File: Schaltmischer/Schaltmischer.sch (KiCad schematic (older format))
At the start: 17 parts, among them P1 Power, P2 IN, P3 Takt, P4 OUT, P5 GND, P6 GND, P7 GND, P8 GND, T1 Übertrager, T2 Übertrager, U1 FST3125

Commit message: Sicherung vor Trafo wechsel im layout
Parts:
- removed C1: 10µ, Discret:C1V7H_2, symbol CP
- removed C2: 10n, Capacitors_SMD:C_1206_HandSoldering, symbol C
- added C1: 10n, Capacitors_SMD:C_1206_HandSoldering, symbol C
- added C2, C3: 1µ, Capacitors_SMD:C_1206_HandSoldering, symbol CP
- added C6: 10µ, Capacitors_SMD:C_1206_HandSoldering, symbol CP
- C5: renamed from C4; value 100n -> 10n
- T1, T2: symbol TRANSFORMER_1P_2S_2 -> TRANSFORMER_SP_1S_2
- renumbered C3 to C4, P5 to P4, P6 to P5, P7 to P6, P8 to P7, P4 to P8, R2 to R1, R1 to R2
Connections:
- net +5V: now also C6.1
- net GND: now also C1.2, C2.2, C3.2, C6.2
- net IN: now also T1.4 (S1); no longer T1.1 (AA)
- net OUT: now also T2.4 (S1); no longer T2.1 (AA)
- net at U1.11 (B), U1.8 (B): now also T2.1 (PR1); no longer T2.5 (SD)
- net at U1.12 (A), U1.2 (A): now also T1.1 (PR1); no longer T1.5 (SD)
- net at C4.1, R1.2, R2.1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: now also C1.1, C2.1, C3.1; no longer T1.4 (SB), T2.4 (SB)
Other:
- moved on the sheet: C4, R2

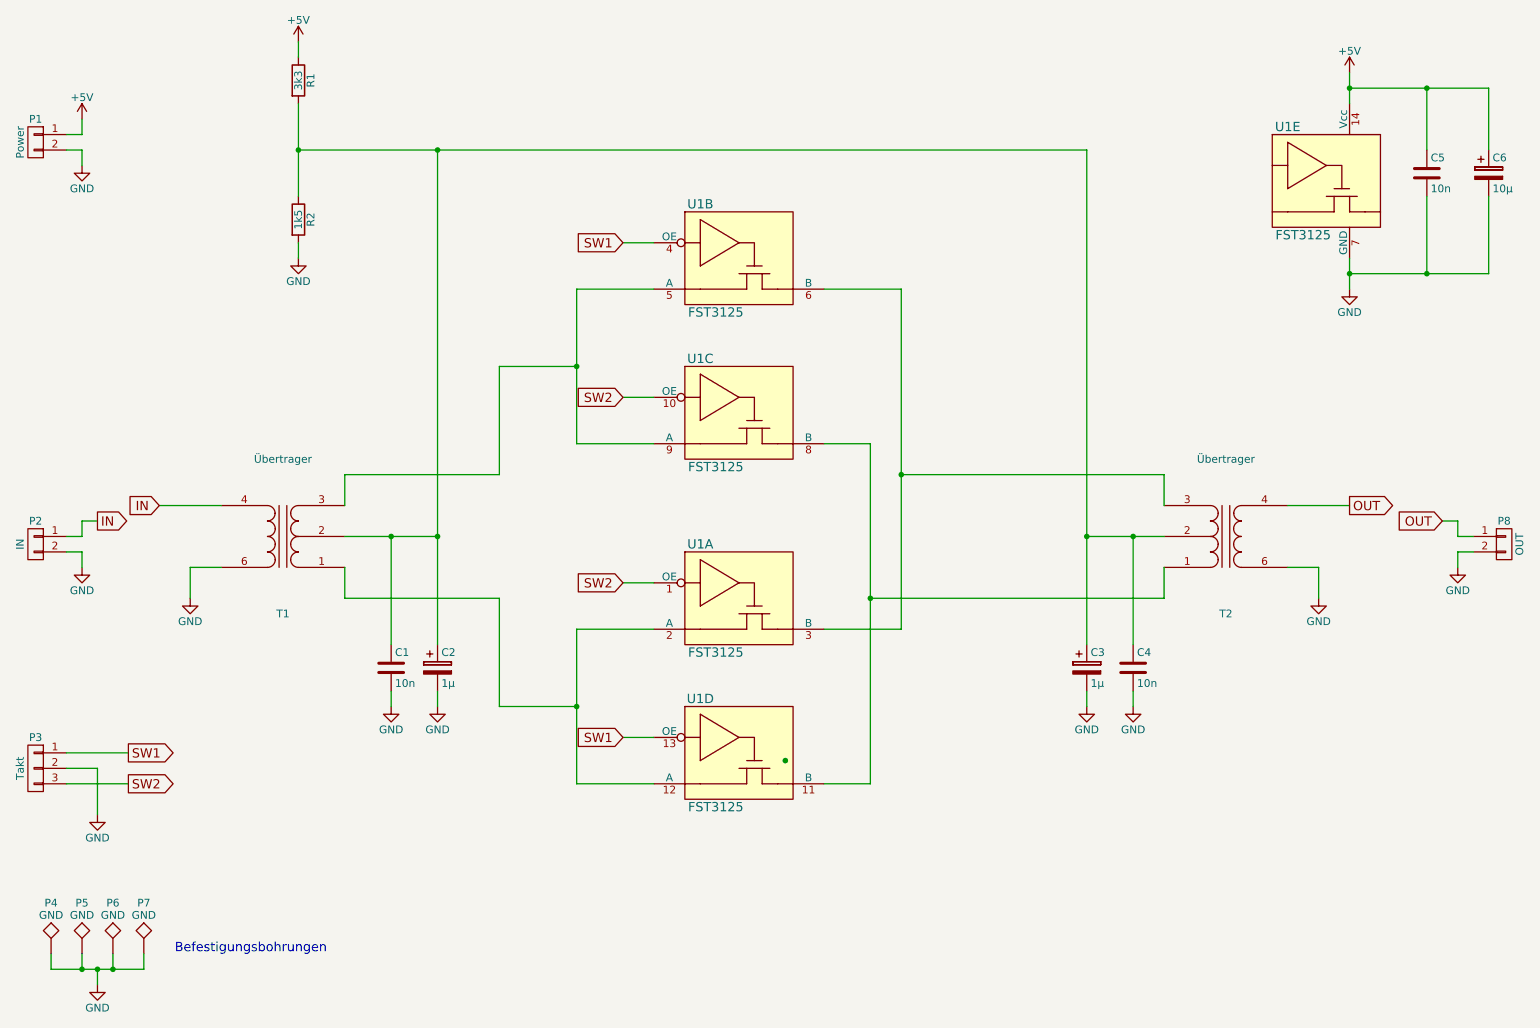
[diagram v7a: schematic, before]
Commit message: Schaltplan Rev E; Layout Rev B
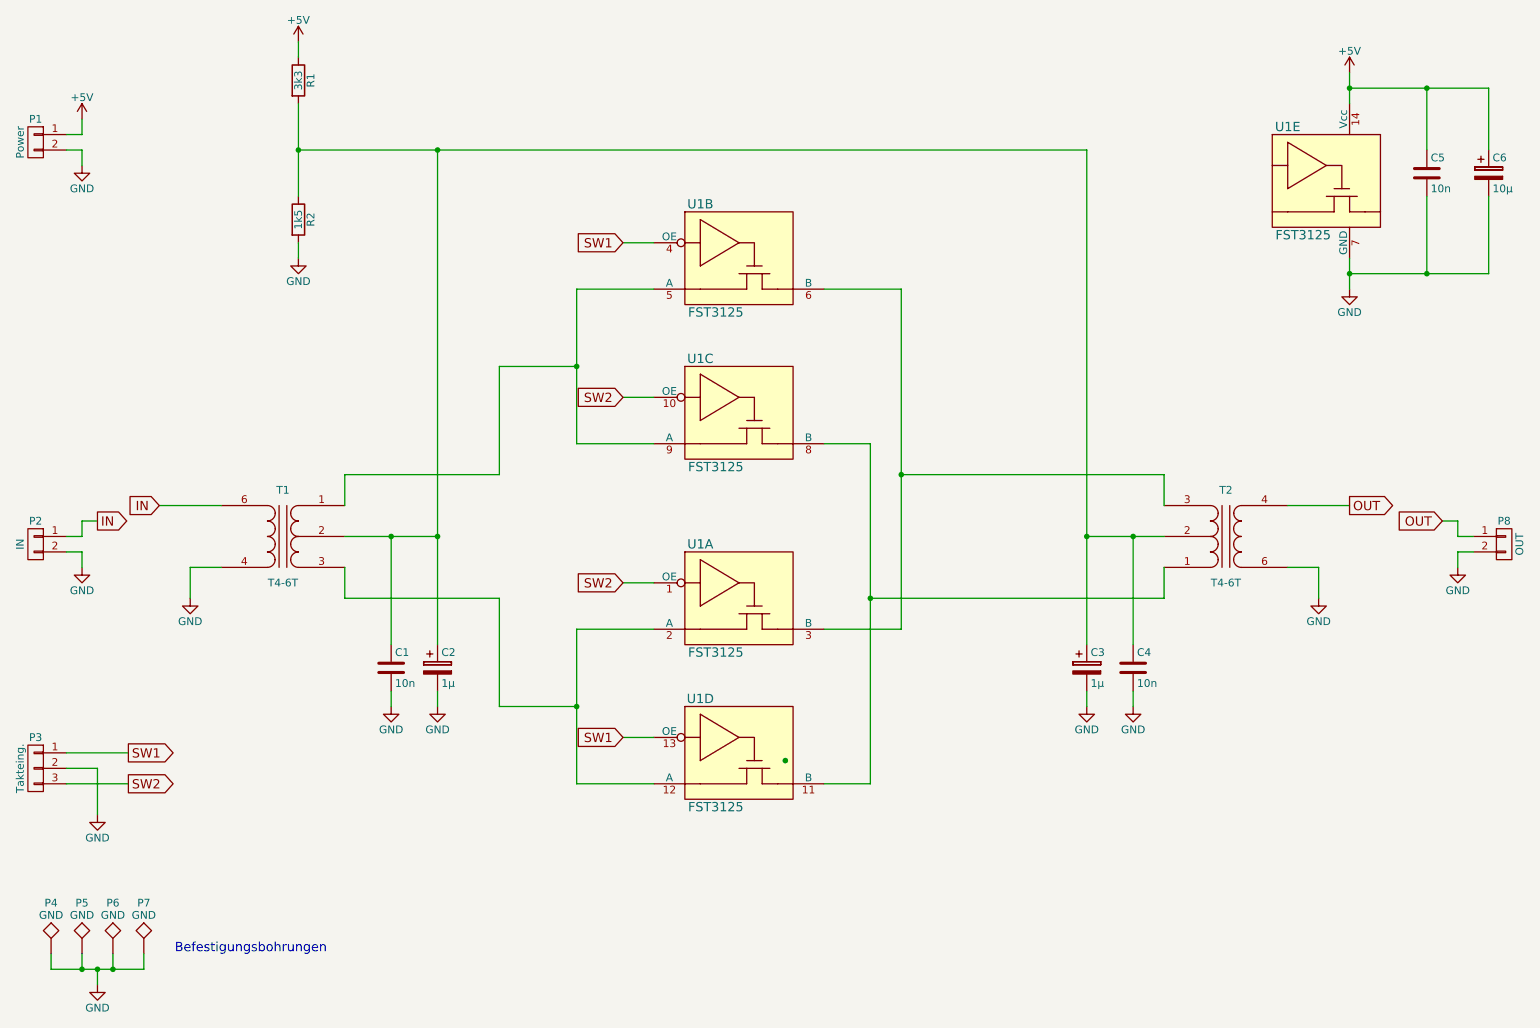
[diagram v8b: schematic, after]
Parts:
- P3: value Takt -> Takteing.
- T1, T2: value Übertrager -> T4-6T
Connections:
- net GND: now also T1.4 (S1); no longer T1.6 (S2)
- net IN: now also T1.6 (S2); no longer T1.4 (S1)
- net at U1.5 (A), U1.9 (A): now also T1.1 (PR1); no longer T1.3 (PR2)
- net at U1.12 (A), U1.2 (A): now also T1.3 (PR2); no longer T1.1 (PR1)
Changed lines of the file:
@@
 Sheet 1 1
 Title "Schaltmischer"
-Date "2018-04-15"
-Rev "D"
+Date "2018-04-16"
+Rev "E"
 Comp "Jonas Gappert"
 Comment1 ""
@@
 U 1 1 5AD25A86
 P 8900 4300
-F 0 "T2" H 8900 4800 50  0000 C CNN
-F 1 "Übertrager" H 8900 3800 50  0000 C CNN
+F 0 "T2" H 8900 4000 50  0000 C CNN
+F 1 "T4-6T" H 8900 4600 50  0000 C CNN
 F 2 "HF_Transformers:T-622" H 8900 4300 50  0001 C CNN
 F 3 "" H 8900 4300 50  0000 C CNN
@@
 P 1200 5800
 F 0 "P3" H 1200 6000 50  0000 C CNN
-F 1 "Takt" V 1300 5800 50  0000 C CNN
+F 1 "Takteing." V 1300 5800 50  0000 C CNN
 F 2 "Pin_Headers:Pin_Header_Straight_1x03_Pitch2.54mm" H 1200 5800 50  0001 C CNN
 F 3 "" H 1200 5800 50  0000 C CNN
@@
 U 1 1 5AD259DF
 P 2800 4300
-F 0 "T1" H 2800 4800 50  0000 C CNN
-F 1 "Übertrager" H 2800 3800 50  0000 C CNN
+F 0 "T1" H 2800 4600 50  0000 C CNN
+F 1 "T4-6T" H 2800 4000 50  0000 C CNN
 F 2 "HF_Transformers:T-622" H 2800 4300 50  0001 C CNN
 F 3 "" H 2800 4300 50  0000 C CNN
 	1    2800 4300
-	-1   0    0    1
-$EndComp
-$Comp
+	-1   0    0    -1
+$EndComp
+$Comp
